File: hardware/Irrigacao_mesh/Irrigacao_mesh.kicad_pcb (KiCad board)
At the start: 2 copper layers, 83 x 99 mm, 96 parts, among them J1 USB_5V_IN, J10 IN0, J11 IN1, J12 IN2, J13 IN3, J14 SENSOR0, J15 SENSOR1, J2 12V_BAT, J4 RTC_PCF8563, J5 UART_PROG, J6 VALVE0, J7 VALVE1, J8 RELAY0_OUT, J9 RELAY1_OUT, K1 FINDER-36.11-5V, K2 FINDER-36.11-5V, Q1 MMBT3904, Q2 MMBT3904, SW1 BOOT/USER, U1 ESP32-WROOM-32, U2 AMS1117-3.3, U3 HT-RA62, U4 L298N, U5 LTV-817, U6 LTV-817, U7 LTV-817, U8 LTV-817

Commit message: Update na placa
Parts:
- added TP1: TestPoint, TestPoint:TestPoint_Pad_D4.0mm, B.Cu at (152.5, 70.5)
- added TP2: TestPoint, TestPoint:TestPoint_Pad_D4.0mm, B.Cu at (152.5, 79.0)
- R20, R21: footprint Resistor_SMD:R_0805_2012Metric -> Resistor_SMD:R_0603_1608Metric
- SW1: footprint Button_Switch_SMD:SW_SPST_TL3305A -> Button_Switch_SMD:SW_Push_1P1T_XKB_TS-1187A
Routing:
- net +5V: track 233.8 -> 235.7 mm, vias 7 -> 8

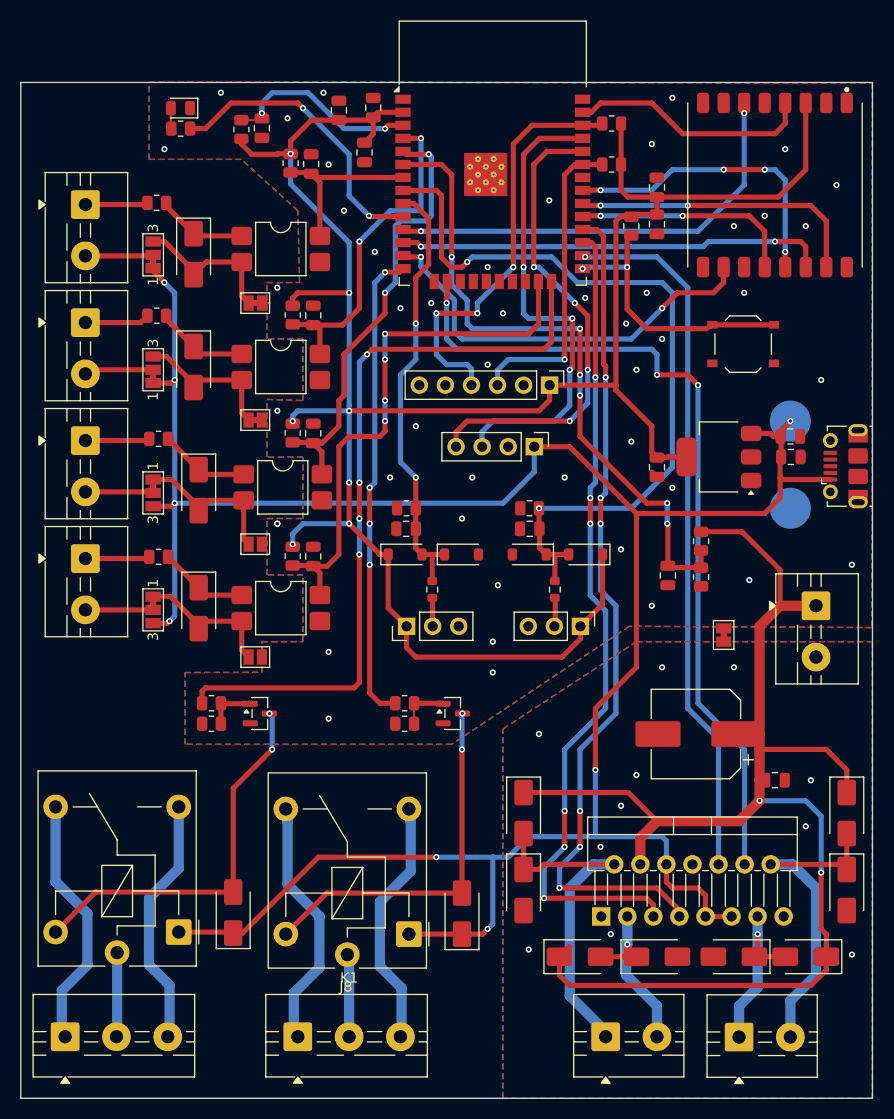
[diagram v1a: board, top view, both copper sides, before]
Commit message: Adição de leds no TX e RX
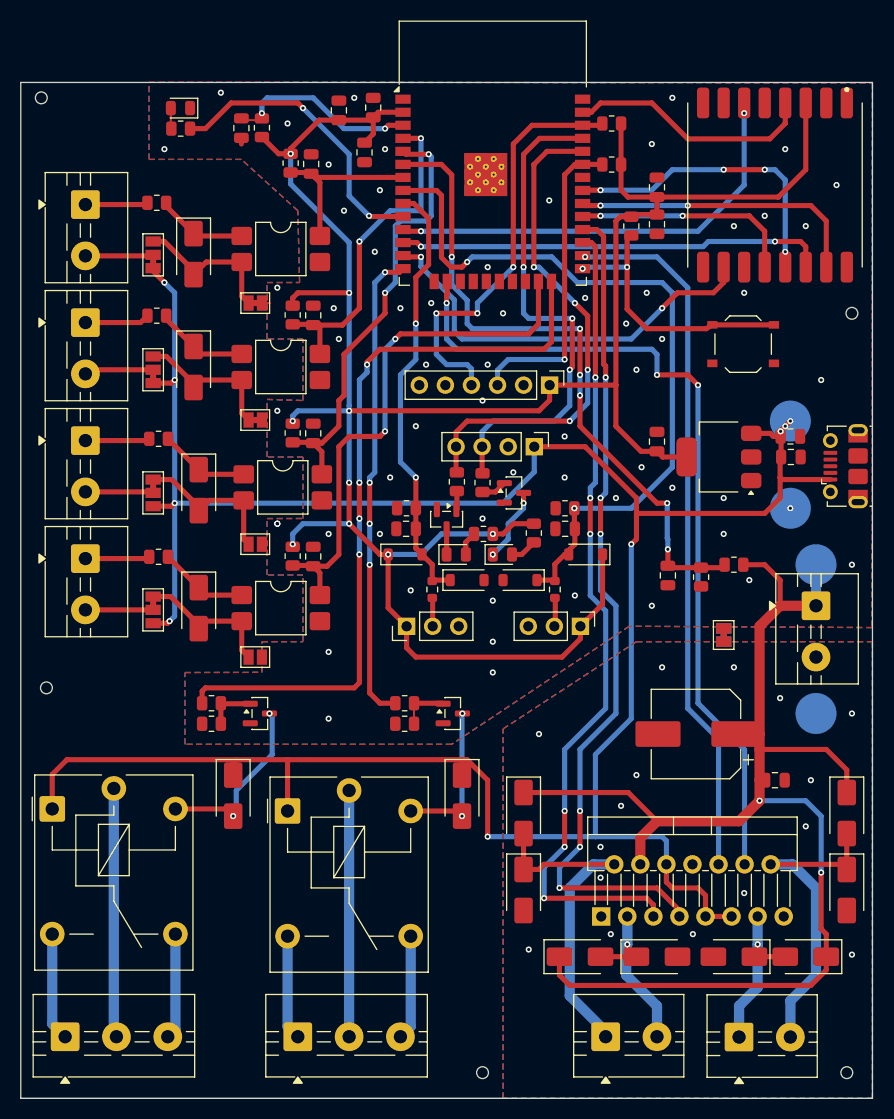
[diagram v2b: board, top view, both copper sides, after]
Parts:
- added D20: LED_TX, LED_SMD:LED_0805_2012Metric, F.Cu at (124.4, 83.5)
- added D22: LED_TX, LED_SMD:LED_0805_2012Metric, F.Cu at (119.9, 83.5)
- added JP10: SolderJumper_2_Bridged, Jumper:SolderJumper-2_P1.3mm_Bridged_Pad1.0x1.5mm, B.Cu at (146.0, 91.3)
- added Q3: MMBT3904, Package_TO_SOT_SMD:SOT-23, F.Cu at (125.6, 77.5)
- added Q4: MMBT3904, Package_TO_SOT_SMD:SOT-23, F.Cu at (119.0, 80.1)
- added R24: 10k, Resistor_SMD:R_0805_2012Metric, F.Cu at (122.5, 76.5)
- added R25: 470, Resistor_SMD:R_0805_2012Metric, F.Cu at (127.5, 81.4)
- added R26: 470, Resistor_SMD:R_0805_2012Metric, F.Cu at (122.6, 81.5)
- added R27: 10k, Resistor_SMD:R_0805_2012Metric, F.Cu at (120.0, 76.4)
- added REF**: ToolingHole_1.152mm, MountingHole:ToolingHole_1.152mm, F.Cu at (80.0, 96.5)
- added REF**: ToolingHole_1.152mm, MountingHole:ToolingHole_1.152mm, F.Cu at (122.5, 134.0)
- added REF**: ToolingHole_1.152mm, MountingHole:ToolingHole_1.152mm, F.Cu at (158.0, 134.0)
- added REF**: ToolingHole_1.152mm, MountingHole:ToolingHole_1.152mm, F.Cu at (158.5, 60.0)
- added REF**: ToolingHole_1.152mm, MountingHole:ToolingHole_1.152mm, F.Cu at (79.5, 39.0)
- added TP3: TestPoint, TestPoint:TestPoint_Pad_D4.0mm, B.Cu at (155.0, 84.5)
- added TP4: TestPoint, TestPoint:TestPoint_Pad_D4.0mm, B.Cu at (155.0, 99.0)
- moved K1 17.2 mm to (80.6, 108.3), turned to 0 degrees
- moved K2 16.8 mm to (103.5, 108.5), turned to 0 degrees
- moved D11 11.5 mm to (120.5, 107.0), turned to -90 degrees
- moved D10 11.4 mm to (98.2, 107.0), turned to -90 degrees
- moved R4 3.94 mm to (147.0, 84.5), turned to 180 degrees
- moved C17 3.45 mm to (130.6, 81.0)
- moved R23 3.45 mm to (130.5, 79.0)
- moved D17 2.66 mm to (126.2, 86.0)
- moved D19 2.56 mm to (121.0, 86.0)
- moved C6 2.50 mm to (139.5, 72.5), turned to 90 degrees
- moved R1 2.01 mm to (101.0, 41.9)
- moved C1 2.00 mm to (99.0, 42.0)
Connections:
- J8 pad 1: REL0_NC -> REL0_NO
- J8 pad 3: REL0_NO -> REL0_NC
- J9 pad 1: REL1_NC -> REL1_NO
- J9 pad 3: REL1_NO -> REL1_NC
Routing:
- net RC1: track 36.4 -> 15.3 mm
- net RC0: track 38.0 -> 17.6 mm
- net REL0_COM: track 8.23 -> 24.4 mm
- net REL1_COM: track 8.23 -> 24.1 mm
- net REL1_NC: track 26.9 -> 11.6 mm
- net REL1_NO: track 26.5 -> 11.4 mm
- net REL0_NC: track 24.9 -> 10.3 mm
- net REL0_NO: track 24.5 -> 10.5 mm
- net +3V3: track 216.7 -> 230.0 mm, vias 7 -> 9
- net +5V: track 235.7 -> 248.9 mm, vias 8 -> 9
- net TXLED_K: track 0.00 -> 7.24 mm, vias 0 -> 2
- net +12V: track 132.6 -> 129.1 mm
- net SENS0: track 75.9 -> 72.9 mm
- net TXLED_A: track 0.00 -> 2.61 mm
- net UART_TX: track 46.5 -> 49.1 mm
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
